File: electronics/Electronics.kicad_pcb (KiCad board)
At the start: 4 copper layers, 102.4 x 75 mm, 85 parts, among them J1 3mm_pad, J10 215079-4, J11 215079-4, J12 215079-4, J13 3mm_pad, J14 3mm_pad, J15 FTSH-105-XX-X-DV, J16 10118193-0001LF, J2 3mm_pad, J3 3mm_pad, J4 3mm_pad, J5 3mm_pad, J6 3mm_pad, J7 215079-4, J8 215079-4, J9 215079-4, Q1 BUK6Y10-30P, U1 STM32G441KB, U10 CM1223-02SO, U2 MAX14930DASE+, U3 MAX14930DASE+, U4 MAX14930DASE+, U5 DRV8243, U6 DRV8243, U7 DRV8243, U8 TPS54227DDAR, U9 NCP164

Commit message: Allahu akbar
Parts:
- U1: value STM32G441KB -> STM32G441KBT3
- moved J7 57.6 mm to (140.1, 85.1), turned to 180 degrees
- moved C16 23.4 mm to (69.0, 109.5), turned to 90 degrees
- moved R9 17.9 mm to (130.2, 59.9), turned to 0 degrees
- moved R8 17.7 mm to (130.2, 58.4), turned to 0 degrees
- moved J4 17.7 mm to (134.7, 57.1), turned to 180 degrees
- moved J3 17.3 mm to (138.8, 57.1), turned to 0 degrees
- moved J9 16.6 mm to (90.6, 108.0)
- moved U3 16.5 mm to (87.3, 91.5)
- moved C5 16.5 mm to (92.0, 95.4)
- moved C8 16.5 mm to (82.7, 95.7)
- moved R10 16.0 mm to (130.2, 61.4), turned to 0 degrees
- moved J8 15.8 mm to (148.4, 85.1)
- moved C15 15.5 mm to (136.5, 59.6), turned to 180 degrees
- moved C13 12.1 mm to (133.1, 72.1), turned to 270 degrees
- moved U6 7.64 mm to (136.4, 63.9), turned to 0 degrees
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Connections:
- C10 pad 1: Earth -> Vdrive
- C10 pad 2: Vdrive -> Earth
- C13 pad 1: Earth -> Vdrive
- C13 pad 2: Vdrive -> Earth
- C16 pad 1: Earth -> Vdrive
- C16 pad 2: Vdrive -> Earth
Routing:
- net +3V3: track 280.1 -> 0.00 mm, vias 10 -> 0
- net Earth: track 251.1 -> 0.00 mm, vias 20 -> 0
- net Vdrive: track 225.7 -> 0.00 mm
- net /Driver/MOT_sleep: track 146.6 -> 0.00 mm, vias 7 -> 0
- net /Driver/MOT_off: track 137.3 -> 0.00 mm, vias 6 -> 0
- net +5VD: track 136.6 -> 0.00 mm, vias 8 -> 0
- net GND: track 118.2 -> 0.00 mm, vias 24 -> 0
- net /MCU-mot1-enc_2: track 63.4 -> 0.00 mm, vias 2 -> 0
- net /MCU-mot2-enc_2: track 61.0 -> 0.00 mm, vias 2 -> 0
- net /MCU-USB_DP: track 58.2 -> 0.00 mm, vias 4 -> 0
- net /MCU-USB_DM: track 57.7 -> 0.00 mm, vias 4 -> 0
- net /MCU-mot1-enc_1: track 57.3 -> 0.00 mm, vias 2 -> 0
- net /MCU-mot2-enc_1: track 57.0 -> 0.00 mm, vias 2 -> 0
- net /Driver/MOT1en_2: track 55.4 -> 0.00 mm, vias 2 -> 0
- net /MCU-mot3-enc_2: track 53.9 -> 0.00 mm, vias 3 -> 0
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- removed copper zone on F.Cu, net Earth
- removed copper zone on In1.Cu, net Earth
- removed copper zone on In2.Cu, net Earth
- removed copper zone on B.Cu, net GND
- removed copper zone on F.Cu, net GND
- removed copper zone on In1.Cu, net GND
- removed copper zone on In2.Cu, net GND

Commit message: Why are we still here? Just to suffer?
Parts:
- moved J7 55.8 mm to (84.3, 83.5)
- moved C5 5.46 mm to (87.5, 98.5)
- moved C8 5.46 mm to (78.2, 98.8)
- moved U3 5.46 mm to (82.8, 94.5)
- moved C25 5.33 mm to (98.9, 117.5), turned to 270 degrees

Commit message: Updated item locations
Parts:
- L1: footprint Inductor_SMD:L_0603_1608Metric_Pad1.05x0.95mm_HandSolder -> Inductor_SMD:L_7.3x7.3_H4.5
- moved J7 55.8 mm to (136.9, 65.0)
- moved R1 50.5 mm to (93.7, 121.8), turned to 90 degrees
- moved R2 50.1 mm to (96.7, 121.8), turned to 90 degrees
- moved R3 48.7 mm to (87.8, 121.7), turned to 90 degrees
- moved R4 47.0 mm to (90.7, 121.7), turned to 90 degrees
- moved D1 45.6 mm to (93.6, 118.2), turned to 90 degrees
- moved J13 45.6 mm to (67.2, 112.3), turned to 0 degrees
- moved D2 45.1 mm to (96.7, 118.2), turned to 90 degrees
- moved D3 44.4 mm to (87.8, 118.2), turned to 90 degrees
- moved J14 43.1 mm to (67.2, 108.3), turned to 180 degrees
- moved D4 42.5 mm to (90.7, 118.2), turned to 90 degrees
- moved Q1 38.0 mm to (72.0, 110.0), turned to 270 degrees
- moved C19 25.3 mm to (98.8, 70.2), turned to 0 degrees
- moved J6 25.3 mm to (65.8, 98.0), turned to 90 degrees
- moved J5 24.2 mm to (65.8, 101.6), turned to 90 degrees
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
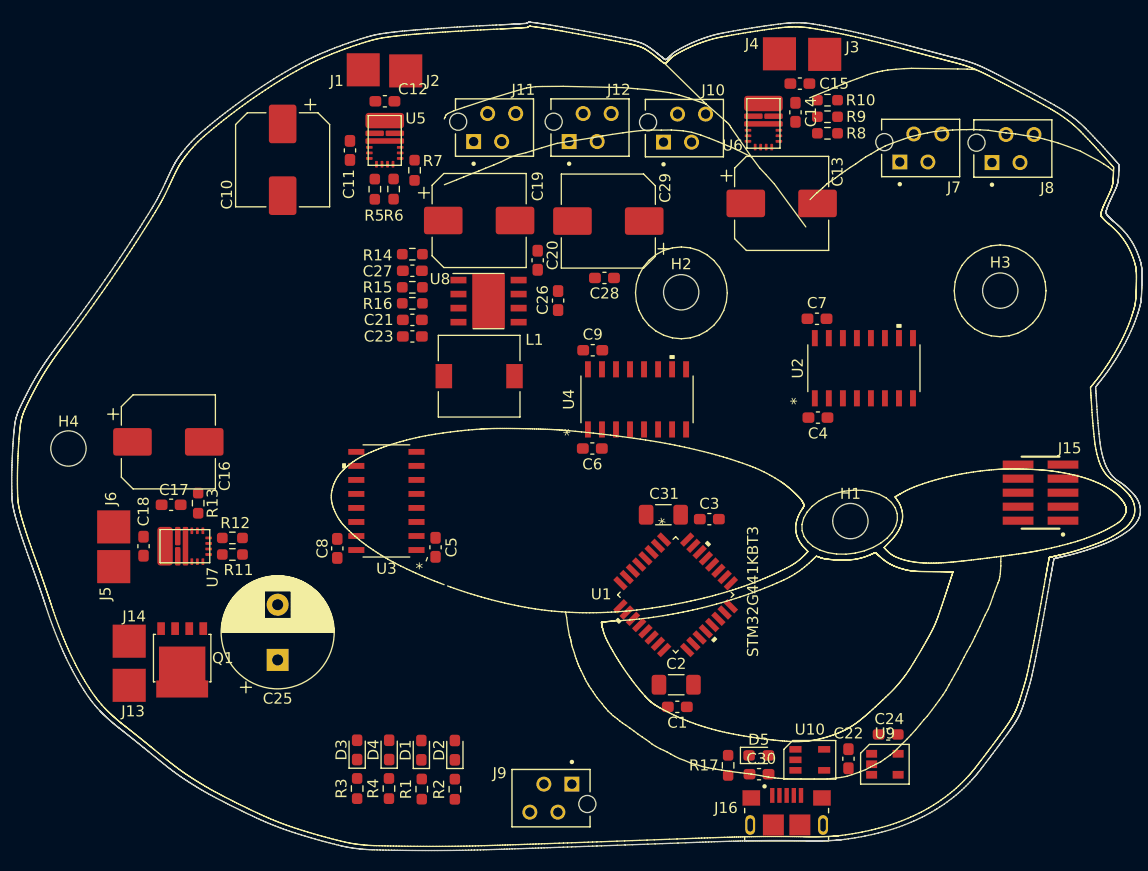
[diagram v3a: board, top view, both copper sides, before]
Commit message: Started drawing new traces
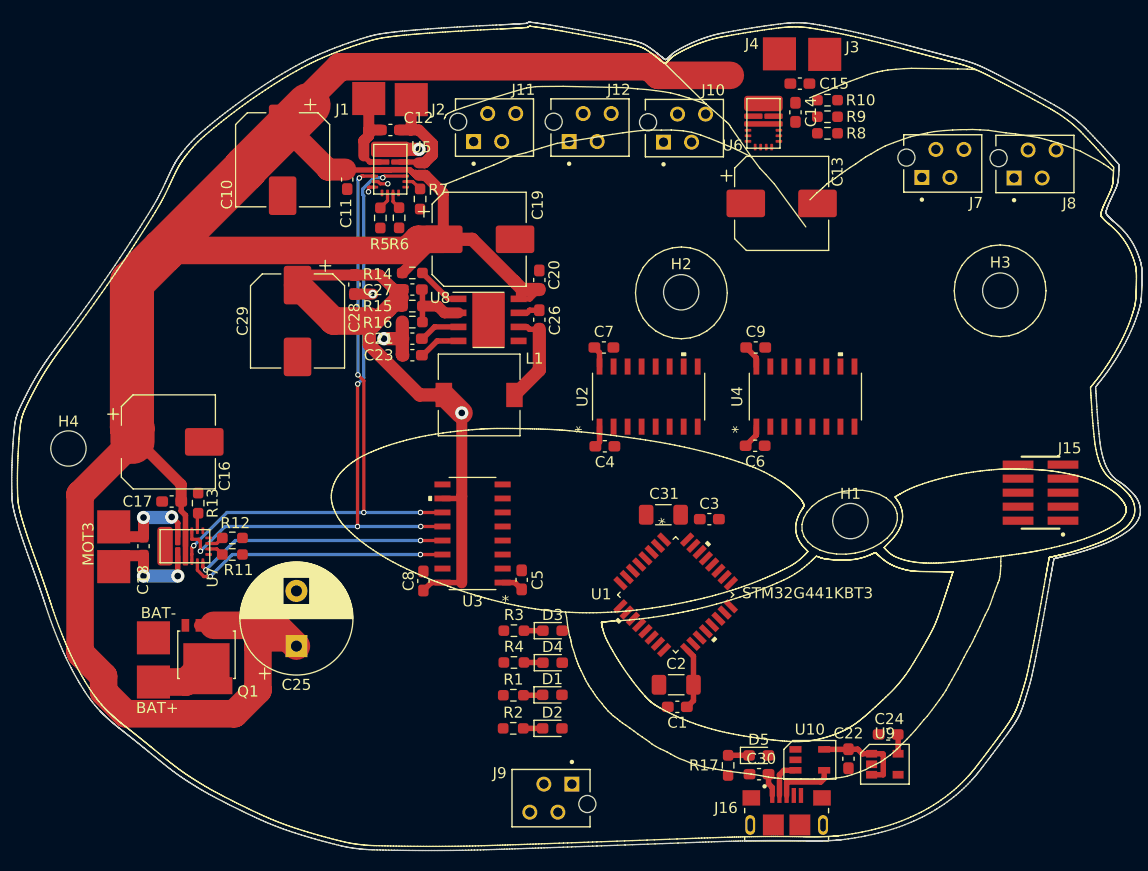
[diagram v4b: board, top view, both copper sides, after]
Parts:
- moved C29 29.6 mm to (82.4, 79.3), turned to 270 degrees
- moved C28 22.7 mm to (87.5, 76.0), turned to 90 degrees
- moved D3 20.7 mm to (105.5, 107.4), turned to 0 degrees
- moved R3 20.2 mm to (102.0, 107.4), turned to 0 degrees
- moved U2 19.7 mm to (114.2, 86.2)
- moved C4 19.5 mm to (110.2, 90.7)
- moved C7 19.5 mm to (110.2, 81.8)
- moved D4 16.8 mm to (105.5, 110.3), turned to 0 degrees
- moved R4 16.1 mm to (102.0, 110.3), turned to 0 degrees
- moved U4 15.3 mm to (128.4, 86.2)
- moved C9 14.8 mm to (123.9, 81.8)
- moved C6 14.8 mm to (123.8, 90.7)
- moved D1 12.9 mm to (105.5, 113.2), turned to 0 degrees
- moved R1 11.9 mm to (102.0, 113.2), turned to 0 degrees
- moved D2 9.04 mm to (105.5, 116.2), turned to 0 degrees
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- renumbered J13 to BAT+, J14 to BAT-, J6 to MOT3, J5 to MOT3
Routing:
- net Vdrive: track 0.00 -> 217.7 mm
- net +5VD: track 0.00 -> 69.8 mm, vias 0 -> 1
- net /Driver/MOT_sleep: track 0.00 -> 60.6 mm, vias 0 -> 5
- net /Driver/MOT_off: track 0.00 -> 57.3 mm, vias 0 -> 5
- net /Driver/MOT3en_1: track 0.00 -> 24.0 mm, vias 0 -> 2
- net /Driver/MOT3en_2: track 0.00 -> 23.4 mm, vias 0 -> 2
- net Net-(C12-Pad2): track 0.00 -> 15.1 mm
- net +3V3: track 0.00 -> 13.5 mm
- net +5VL: track 0.00 -> 10.5 mm
- net Earth: track 0.00 -> 10.1 mm, vias 0 -> 3
- net Net-(C18-Pad1): track 0.00 -> 9.92 mm, vias 0 -> 2
- net Net-(C18-Pad2): track 0.00 -> 9.68 mm, vias 0 -> 2
- net Net-(C26-Pad2): track 0.00 -> 8.85 mm
- net Net-(C12-Pad1): track 0.00 -> 8.20 mm
- net Net-(C27-Pad1): track 0.00 -> 6.49 mm
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
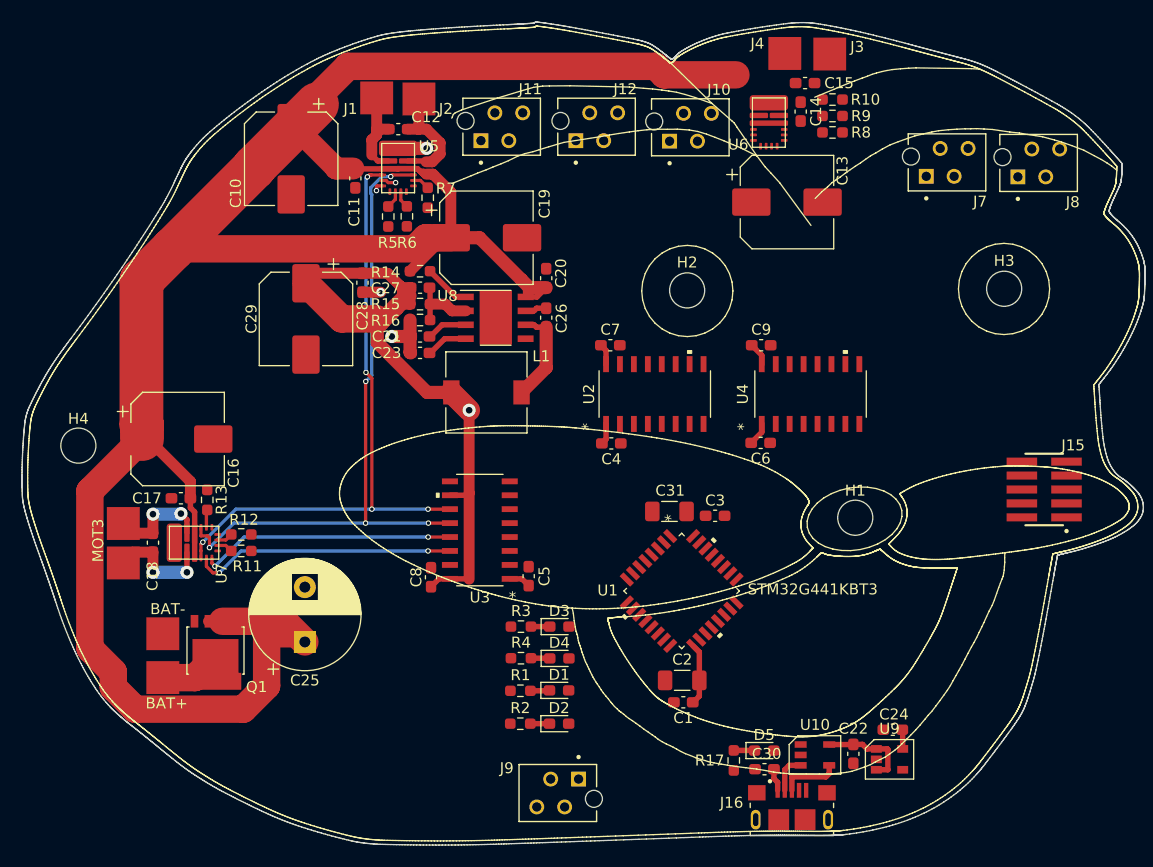
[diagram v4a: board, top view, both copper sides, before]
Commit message: Motor connections done
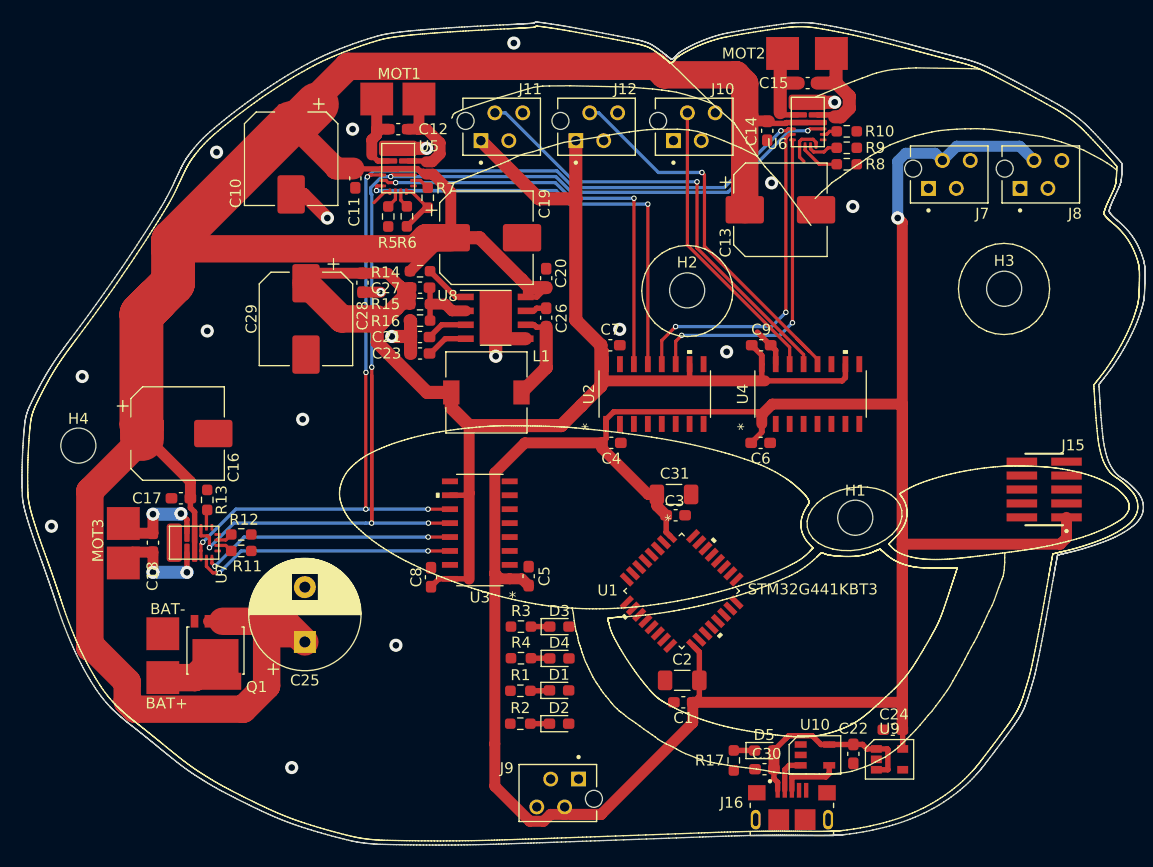
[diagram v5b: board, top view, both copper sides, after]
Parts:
- moved MOT2 4.30 mm to (125.8, 55.1)
- moved J4 4.25 mm to (130.3, 55.1)
- moved C3 3.60 mm to (116.1, 97.2), turned to 0 degrees
- moved U6 3.55 mm to (128.2, 61.4)
- moved C14 3.52 mm to (124.5, 62.2), turned to 90 degrees
- moved R10 3.18 mm to (131.7, 62.2)
- moved R8 3.18 mm to (131.7, 65.2)
- moved R9 3.18 mm to (131.7, 63.8)
- moved C31 1.60 mm to (116.0, 95.3)
- moved J7 1.12 mm to (139.2, 67.5)
- moved J8 1.07 mm to (147.5, 67.5)
- moved C13 0.92 mm to (125.7, 69.4)
- moved C16 0.50 mm to (70.7, 89.8)
- moved J10 0.35 mm to (115.9, 63.1)
- moved C15 0.24 mm to (128.1, 57.9), turned to 0 degrees
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- renumbered J1 to MOT1, J3 to MOT2
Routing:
- net +3V3: track 13.5 -> 256.0 mm, vias 0 -> 1
- net +5VD: track 69.8 -> 148.0 mm, vias 1 -> 0
- net /Driver/MOT_sleep: track 60.6 -> 116.2 mm, vias 5 -> 6
- net /Driver/MOT1en_2: track 0.96 -> 54.3 mm, vias 1 -> 2
- net /Hold-serv_PWM: track 0.00 -> 41.7 mm, vias 0 -> 1
- net /Driver/MOT_off: track 57.3 -> 98.9 mm, vias 5 -> 6
- net /Driver/MOT1en_1: track 1.26 -> 38.7 mm, vias 1 -> 2
- net /Aim-serv_PWM: track 0.00 -> 36.5 mm, vias 0 -> 1
- net /Driver/MOT2en_1: track 0.00 -> 31.2 mm, vias 0 -> 2
- net /Driver/MOT2en_2: track 0.00 -> 30.1 mm, vias 0 -> 2
- net Earth: track 10.1 -> 37.2 mm, vias 3 -> 19
- net /TRW_PWM: track 0.00 -> 26.8 mm
- net Vdrive: track 217.7 -> 239.0 mm
- net Net-(C15-Pad2): track 0.00 -> 11.1 mm
- net Net-(C15-Pad1): track 0.00 -> 8.79 mm
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- added copper zone on In1.Cu, net Earth
- added copper zone on In2.Cu, net Earth

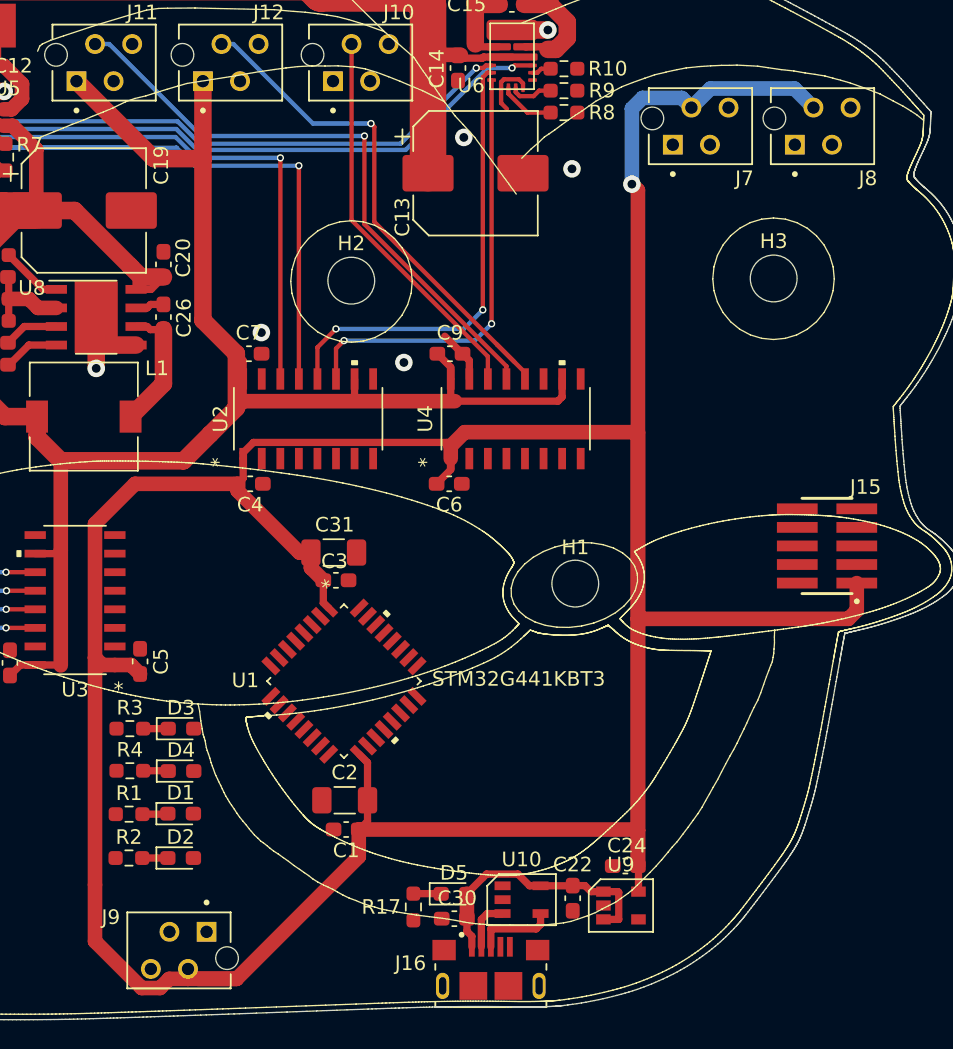
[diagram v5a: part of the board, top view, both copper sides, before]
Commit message: MCU connections done v2
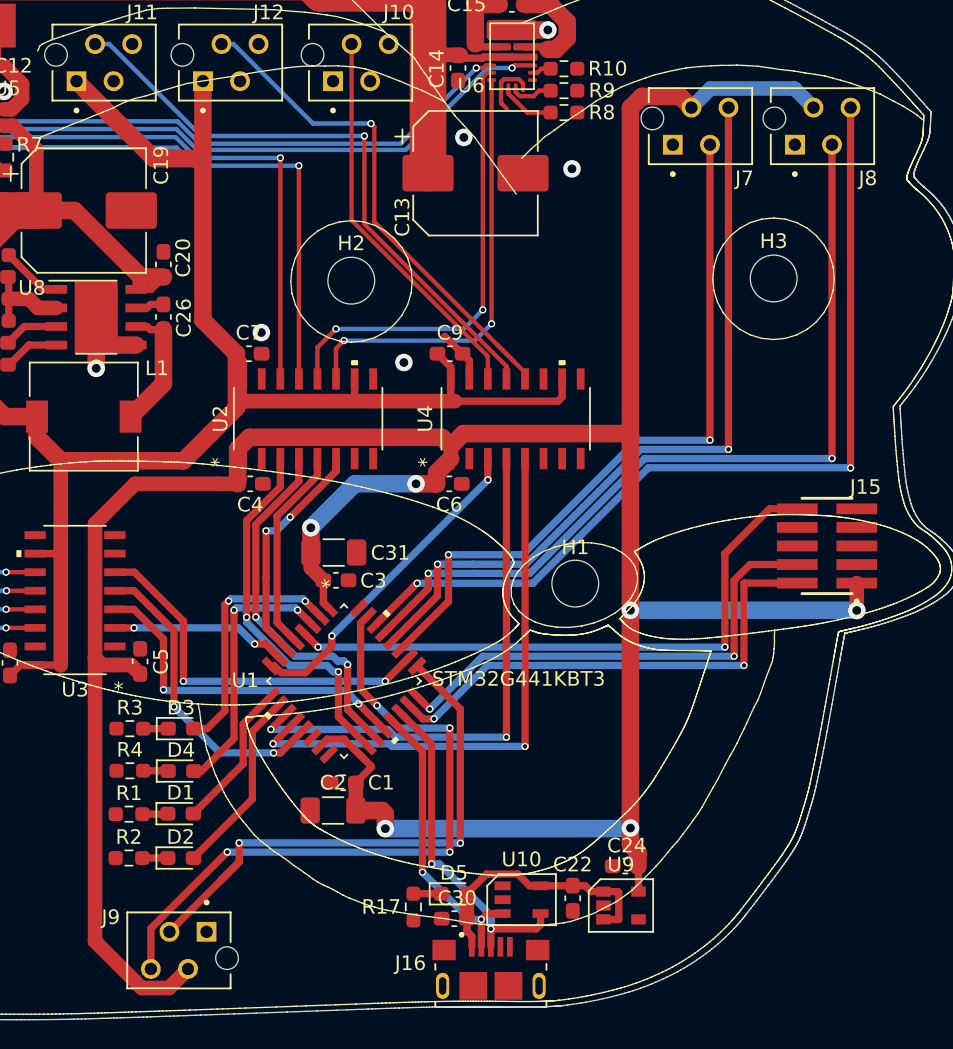
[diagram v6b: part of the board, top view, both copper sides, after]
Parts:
- moved C1 3.21 mm to (116.6, 111.1)
- moved C2 1.06 mm to (115.9, 113.0)
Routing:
- net /MCU-mot2-enc_2: track 0.00 -> 61.6 mm, vias 0 -> 2
- net /MCU-mot2-enc_1: track 0.00 -> 57.7 mm, vias 0 -> 2
- net /MCU-mot1-enc_2: track 0.00 -> 53.1 mm, vias 0 -> 2
- net /MCU-mot1-enc_1: track 0.00 -> 49.2 mm, vias 0 -> 2
- net /MCU-mot3-enc_2: track 0.00 -> 46.3 mm, vias 0 -> 4
- net /MCU_NRST: track 0.00 -> 41.8 mm, vias 0 -> 2
- net +3V3: track 256.0 -> 215.6 mm, vias 1 -> 6
- net /MCU-Aim-serv_PWM: track 0.00 -> 39.2 mm, vias 0 -> 2
- net /MCU-mot3-enc_1: track 0.00 -> 38.2 mm, vias 0 -> 2
- net /MCU-Hold-serv_PWM: track 0.00 -> 37.0 mm, vias 0 -> 2
- net /MCU_SWDIO: track 0.00 -> 34.1 mm, vias 0 -> 2
- net /MCU_SWCLK: track 0.00 -> 33.5 mm, vias 0 -> 2
- net /MCU-mot_off: track 0.00 -> 26.3 mm, vias 0 -> 2
- net /MCU-MOT1en_1: track 0.00 -> 25.7 mm, vias 0 -> 2
- net /MCU-MOT1en_2: track 0.00 -> 25.5 mm, vias 0 -> 2
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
